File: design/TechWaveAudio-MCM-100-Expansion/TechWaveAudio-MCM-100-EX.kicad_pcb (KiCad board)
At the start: 2 copper layers, 10 x 110 mm, 19 parts, among them J21 Expansion, J22 xCV1, J23 xCV2, J24 xCV3, J25 xCV4, U1 DAC7554, U2 TL072, U3 TL072

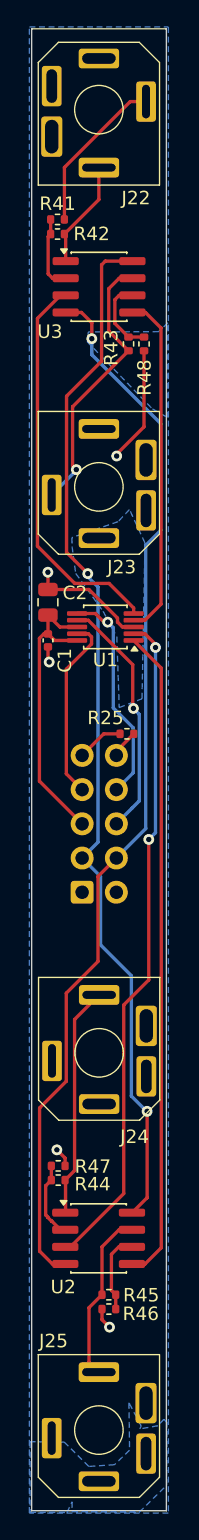
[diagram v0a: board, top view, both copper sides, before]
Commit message: update expansion;  ensure ex state is properly set
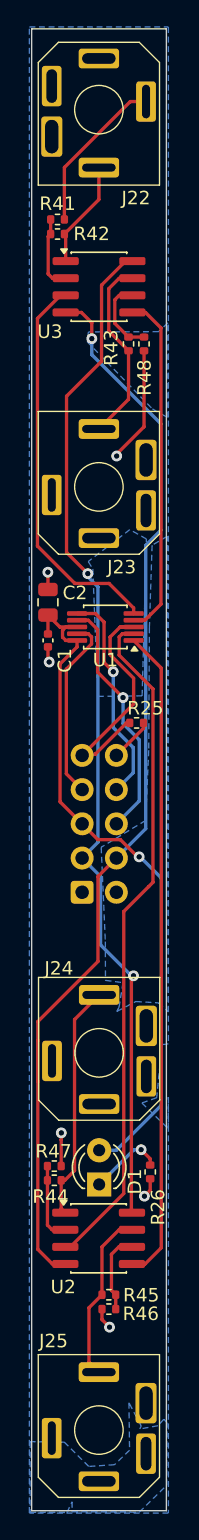
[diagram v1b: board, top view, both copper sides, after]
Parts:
- added D1: LED, LED_THT:LED_D3.0mm, F.Cu at (136.1, 120.7)
- added R26: 1k, Resistor_SMD:R_0402_1005Metric, F.Cu at (139.9, 119.8)
- moved R25 1.08 mm to (138.9, 86.4)
- moved R44 0.29 mm to (132.8, 120.4)
- moved R47 0.29 mm to (132.8, 119.3)
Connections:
- J23 pad 1: Net-(J23-Pin_1) -> GND
- J23 pad 2: GND -> Net-(J23-Pin_2)
- R43 pad 1: Net-(J23-Pin_1) -> Net-(J23-Pin_2)
- U3 pad 7: Net-(J23-Pin_1) -> Net-(J23-Pin_2)
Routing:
- net +5V: track 22.1 -> 51.2 mm, vias 0 -> 1
- net Net-(J23-Pin_1): track 20.6 -> 0.00 mm, vias 1 -> 0
- net Net-(J23-Pin_2): track 0.00 -> 14.0 mm
- net GND: track 37.2 -> 46.2 mm, vias 5 -> 6
- net Net-(D1-K): track 0.00 -> 5.60 mm, vias 0 -> 1
- net +12V: track 77.8 -> 76.2 mm
- net ExpSense: track 1.83 -> 3.24 mm
- net Net-(U1-VOUTB): track 49.3 -> 50.0 mm, vias 2 -> 0
